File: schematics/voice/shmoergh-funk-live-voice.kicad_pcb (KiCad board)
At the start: 2 copper layers, 40 x 42 mm, 25 parts, among them Q1 2N3904, U1 TL074

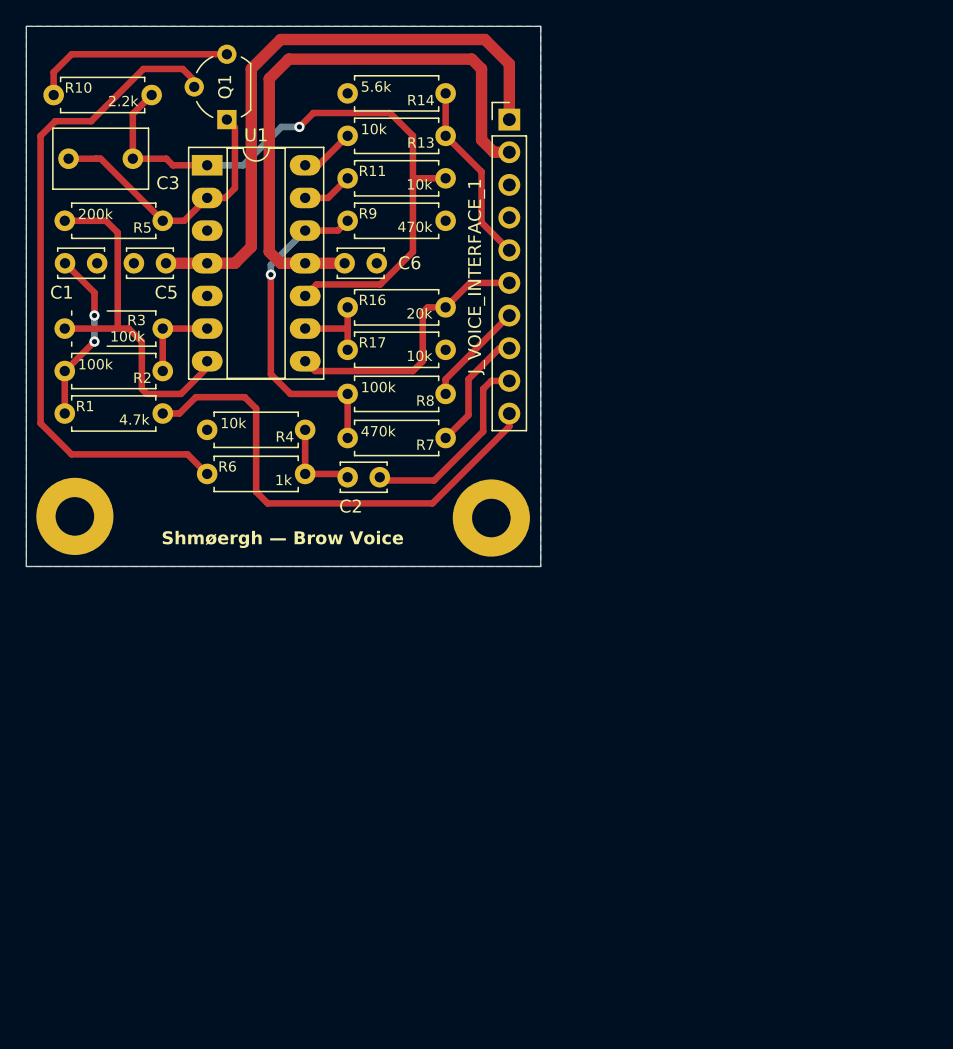
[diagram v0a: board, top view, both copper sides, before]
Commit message: Added digital ADSR (untested)
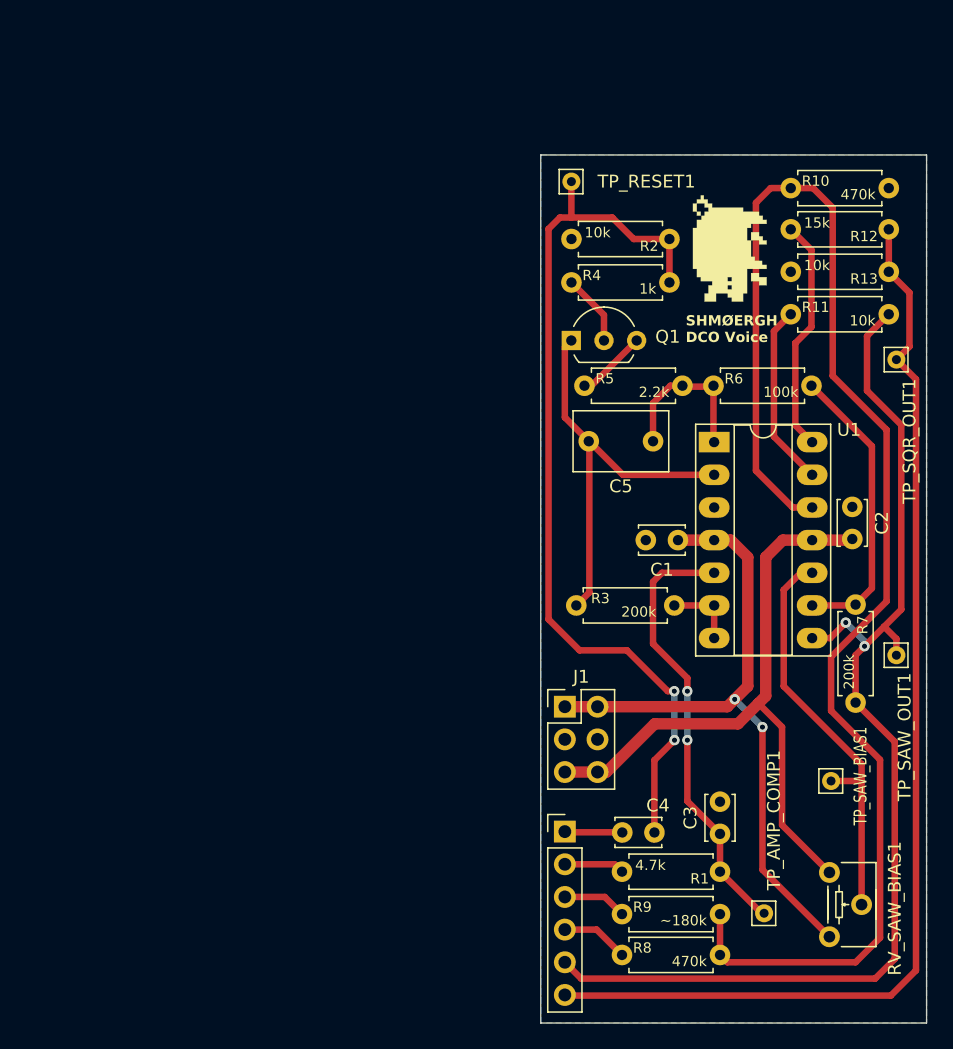
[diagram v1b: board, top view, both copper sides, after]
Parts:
- removed C6: 100n, Capacitor_THT:C_Disc_D3.4mm_W2.1mm_P2.50mm
- removed H1, H2: MountingHole, MountingHole:MountingHole_3mm_Pad
- removed R14: 5.6k, Shmoergh_Custom_Footprints:R_Axial_DIN0207_L6.3mm_D2.5mm_P7.62mm_Horizontal
- removed R16: 20k, Shmoergh_Custom_Footprints:R_Axial_DIN0207_L6.3mm_D2.5mm_P7.62mm_Horizontal
- removed R17: 10k, Shmoergh_Custom_Footprints:R_Axial_DIN0207_L6.3mm_D2.5mm_P7.62mm_Horizontal
- added C4: 560, Capacitor_THT:C_Disc_D3.4mm_W2.1mm_P2.50mm, F.Cu at (133.8, 102.7)
- added G***: LOGO, Shmoergh_Custom_Footprints:Gyeszno, F.Cu at (139.7, 57.3)
- added J1: Power, Connector_PinHeader_2.54mm:PinHeader_2x03_P2.54mm_Vertical, F.Cu at (126.9, 92.9)
- added R12: 15k, Shmoergh_Custom_Footprints:R_Axial_DIN0207_L6.3mm_D2.5mm_P7.62mm_Horizontal, F.Cu at (152.1, 55.8)
- added RV_SAW_BIAS1: 10k fine, PCM_Potentiometer_THT_AKL:Potentiometer_ACP_CA6-H2,5_Horizontal, F.Cu at (147.4, 105.8)
- added TP_AMP_COMP1: TestPoint, Connector_Pin:Pin_D0.7mm_L6.5mm_W1.8mm_FlatFork, F.Cu at (142.4, 109.0)
- added TP_RESET1: TestPoint, Connector_Pin:Pin_D0.7mm_L6.5mm_W1.8mm_FlatFork, F.Cu at (127.4, 52.1)
- added TP_SAW_BIAS1: TestPoint, Connector_Pin:Pin_D0.7mm_L6.5mm_W1.8mm_FlatFork, F.Cu at (147.6, 98.7)
- added TP_SAW_OUT1: TestPoint, Connector_Pin:Pin_D0.7mm_L6.5mm_W1.8mm_FlatFork, F.Cu at (152.7, 88.9)
- added TP_SQR_OUT1: TestPoint, Connector_Pin:Pin_D0.7mm_L6.5mm_W1.8mm_FlatFork, F.Cu at (152.7, 65.9)
- C2: value 270p -> 100n
- C3: value 1n (foil) -> 100n; footprint Capacitor_THT:C_Rect_L7.2mm_W4.5mm_P5.00mm_FKS2_FKP2_MKS2_MKP2 -> Capacitor_THT:C_Disc_D3.4mm_W2.1mm_P2.50mm
- C5: value 100n -> 1n (foil); footprint Capacitor_THT:C_Disc_D3.4mm_W2.1mm_P2.50mm -> Capacitor_THT:C_Rect_L7.2mm_W4.5mm_P5.00mm_FKS2_FKP2_MKS2_MKP2
- J_VOICE_INTERFACE_1: value Conn_01x10 -> Conn_01x06; footprint Connector_PinHeader_2.54mm:PinHeader_1x10_P2.54mm_Vertical -> Connector_PinHeader_2.54mm:PinHeader_1x06_P2.54mm_Vertical
- Q1: value 2N3904 -> 2N3906; footprint Package_TO_SOT_THT:TO-92_Wide -> PCM_Package_TO_SOT_THT_AKL:TO-92L_Inline_Wide
- R10: value 2.2k -> 470k
- R2: value 100k -> 10k
- R3: value 100k -> 200k
- R4: value 10k -> 1k
- R5: value 200k -> 2.2k
- R6: value 1k -> 100k
- R7: value 470k -> 200k
- R8: value 100k -> 470k
- R9: value 470k -> ~180k
- moved C3 69.6 mm to (138.9, 102.8), turned to 90 degrees
- moved R1 62.2 mm to (138.9, 105.7), turned to 180 degrees
- moved R9 58.0 mm to (131.3, 109.0)
- moved R10 57.8 mm to (144.4, 52.6)
- moved J_VOICE_INTERFACE_1 55.5 mm to (126.9, 102.6)
- moved C1 52.3 mm to (135.7, 80.0), turned to 180 degrees
- moved R8 45.7 mm to (131.3, 112.2), turned to 0 degrees
- moved R3 45.2 mm to (127.8, 85.0)
- moved U1 44.9 mm to (138.5, 72.3)
- moved R2 40.7 mm to (135.0, 56.5)
- moved C5 40.3 mm to (133.7, 72.3)
- moved R6 40.0 mm to (138.4, 67.9)
- moved C2 39.3 mm to (149.2, 77.4), turned to -90 degrees
- moved R11 36.0 mm to (144.4, 62.4)
- moved R13 36.0 mm to (152.1, 59.1)
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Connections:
- C1 pad 1: Net-(C1-Pad1) -> +12V
- C2 pad 1: Net-(C2-Pad1) -> GND
- C2 pad 2: RESET -> -12V
- C3 pad 1: Net-(U1C-+) -> Net-(U1B-+)
- C3 pad 2: Net-(Q1-E) -> GND
- C5 pad 1: +12V -> Net-(C5-Pad1)
- C5 pad 2: GND -> Net-(Q1-E)
- J_VOICE_INTERFACE_1 pad 1: +12V -> RESET
- J_VOICE_INTERFACE_1 pad 2: -12V -> AMP
- J_VOICE_INTERFACE_1 pad 3: GND -> PULSE_WIDTH
- J_VOICE_INTERFACE_1 pad 4: unconnected-(J_VOICE_INTERFACE_1-Pin_4-Pad4) -> PWM
- J_VOICE_INTERFACE_1 pad 5: SQR_OUT -> SAW_OUT
- J_VOICE_INTERFACE_1 pad 6: SAW_OUT -> SQR_OUT
- R1 pad 1: Net-(C1-Pad1) -> Net-(U1B-+)
- R10 pad 1: Net-(Q1-C) -> Net-(U1D-+)
- R10 pad 2: Net-(U1C-+) -> GND
- R11 pad 2: Net-(U1C-+) -> SAW_OUT
- R13 pad 2: Net-(R13-Pad2) -> GND
- R2 pad 1: Net-(U1B--) -> Net-(C4-Pad1)
- R2 pad 2: Net-(C1-Pad1) -> GND
- R3 pad 1: Net-(R3-Pad1) -> Net-(Q1-E)
- R4 pad 1: Net-(C2-Pad1) -> Net-(Q1-B)
- R4 pad 2: GND -> Net-(C4-Pad1)
- R5 pad 1: Net-(Q1-E) -> Net-(Q1-C)
- R5 pad 2: Net-(R3-Pad1) -> Net-(C5-Pad1)
- R6 pad 1: Net-(Q1-B) -> Net-(C5-Pad1)
- R6 pad 2: Net-(C2-Pad1) -> Net-(U1C--)
- R7 pad 1: PWM -> Net-(U1C--)
- R7 pad 2: Net-(U1D-+) -> SAW_OUT
- R8 pad 1: PULSE_WIDTH -> PWM
- R9 pad 1: Net-(U1D-+) -> PULSE_WIDTH
- R9 pad 2: GND -> Net-(U1D-+)
- U1 pad 1: Net-(U1C-+) -> Net-(C5-Pad1)
- U1 pad 14: Net-(R13-Pad2) -> Net-(R12-Pad2)
- U1 pad 5: GND -> Net-(U1B-+)
- U1 pad 7: Net-(R3-Pad1) -> Net-(U1B--)
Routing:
- net Net-(U1D-+): track 25.9 -> 112.0 mm, vias 1 -> 0
- net SQR_OUT: track 14.2 -> 87.5 mm
- net Net-(C4-Pad1): track 0.00 -> 70.7 mm, vias 0 -> 2
- net SAW_OUT: track 21.3 -> 89.7 mm, vias 0 -> 2
- net Net-(Q1-B): track 51.9 -> 5.56 mm
- net Net-(U1B-+): track 0.00 -> 34.5 mm, vias 0 -> 2
- net AMP: track 38.2 -> 4.68 mm
- net Net-(R3-Pad1): track 28.7 -> 0.00 mm
- net Net-(U1C-+): track 51.2 -> 32.1 mm, vias 1 -> 0
- net Net-(R12-Pad2): track 0.00 -> 18.3 mm
- net Net-(U1C--): track 6.60 -> 22.9 mm
- net Net-(C1-Pad1): track 13.6 -> 0.00 mm, vias 2 -> 0
- net Net-(C5-Pad1): track 0.00 -> 12.7 mm
- net Net-(Q1-E): track 21.6 -> 32.9 mm
- net RESET: track 15.3 -> 4.49 mm
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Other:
- board size 40 x 42 mm -> 30 x 67.5 mm
- board text added: "SHMØERGH DCO Voice"
- board text removed: "Shmøergh — Brow Voice"

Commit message: Updated schem. + added JLCPCB gerbers
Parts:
- removed G***: LOGO, Shmoergh_Custom_Footprints:Gyeszno
- R10: value 470k -> 330k
- R11: value 10k -> 100k
- R9: value ~180k -> 470k
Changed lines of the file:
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@@
         (effects (font (size 0.8 0.8) (thickness 0.15)) (justify left))
     )
-    (fp_text value "470k" (at 6.6 0.5) (layer "F.SilkS")
+    (fp_text value "330k" (at 6.6 0.5) (layer "F.SilkS")
         (effects (font (size 0.8 0.8) (thickness 0.15)) (justify right))
     )
@@
         (effects (font (size 0.8 0.8) (thickness 0.15)) (justify left))
     )
-    (fp_text value "10k" (at 6.6 0.5) (layer "F.SilkS")
+    (fp_text value "100k" (at 6.6 0.5) (layer "F.SilkS")
         (effects (font (size 0.8 0.8) (thickness 0.15)) (justify right))
     )
@@
     )
   )
-  (footprint "Shmoergh_Custom_Footprints:Gyeszno" (layer "F.Cu")
-    (at 139.7 57.277 90)
-    (attr through_hole)
-    (fp_text reference "G***" (at 0 0 90) (layer "F.SilkS") hide
-        (effects (font (size 1.524 1.524) (thickness 0.3)))
-    )
-    (fp_text value "LOGO" (at 0.75 0 90) (layer "F.SilkS") hide
-        (effects (font (size 1.524 1.524) (thickness 0.3)))
-    )
-    (fp_poly
-      (pts
-        (xy 2.8702 -2.8702)
-        (xy 3.5052 -2.8702)
-        (xy 3.5052 -2.5654)
-        (xy 2.8702 -2.5654)
-        (xy 2.8702 -2.8702)
-      )
-      (stroke (width 0.01) (type solid)) (fill solid) (layer "F.SilkS"))
-    (fp_poly
-      (pts
-        (xy 2.8702 -2.2606)
-        (xy 2.5527 -2.2606)
-        (xy 2.5527 -2.5654)
-        (xy 2.8702 -2.5654)
-        (xy 2.8702 -2.2606)
-      )
-      (stroke (width 0.01) (type solid)) (fill solid) (layer "F.SilkS"))
-    (fp_poly
-      (pts
-        (xy -1.905 2.2733)
-        (xy -2.2225 2.2733)
-        (xy -2.2225 2.8702)
-        (xy -2.8575 2.8702)
-        (xy -2.8575 2.2733)
-        (xy -2.54 2.2733)
-        (xy -2.54 1.651)
-        (xy -1.905 1.651)
-        (xy -1.905 2.2733)
-      )
-      (stroke (width 0.01) (type solid)) (fill solid) (layer "F.SilkS"))
-    (fp_poly
-      (pts
-        (xy 1.27 2.2733)
-        (xy 0.9525 2.2733)
-        (xy 0.9525 2.5654)
-        (xy 0.635 2.5654)
-        (xy 0.635 2.8702)
-        (xy 0.3175 2.8702)
-        (xy 0.3175 2.2733)
-        (xy 0.635 2.2733)
-        (xy 0.635 1.651)
-        (xy 1.27 1.651)
-        (xy 1.27 2.2733)
-      )
-      (stroke (width 0.01) (type solid)) (fill solid) (layer "F.SilkS"))
-    (fp_poly
-      (pts
-        (xy 1.6002 -2.5654)
-        (xy 2.2352 -2.5654)
-        (xy 2.2352 -2.2098)
-        (xy 2.5527 -2.2098)
-        (xy 2.5527 -1.9685)
-        (xy 2.8702 -1.9685)
-        (xy 2.8702 -1.6637)
-        (xy 3.1877 -1.6637)
-        (xy 3.1877 -1.9685)
-        (xy 3.5052 -1.9685)
-        (xy 3.5052 -2.5654)
-        (xy 3.8227 -2.5654)
-        (xy 3.8227 -2.2606)
-        (xy 4.1402 -2.2606)
-        (xy 4.1402 -2.0193)
-        (xy 3.8227 -2.0193)
-        (xy 3.8227 -1.7145)
-        (xy 3.5052 -1.7145)
-        (xy 3.5052 -1.3716)
-        (xy 3.1877 -1.3716)
-        (xy 3.1877 1.0414)
-        (xy 2.8702 1.0414)
-        (xy 2.8702 2.2733)
-        (xy 2.5527 2.2733)
-        (xy 2.5527 2.5654)
-        (xy 2.2352 2.5654)
-        (xy 2.2352 2.8702)
-        (xy 1.9177 2.8702)
-        (xy 1.9177 1.651)
-        (xy 1.6002 1.651)
-        (xy 1.6002 1.3462)
-        (xy 0.635 1.3462)
-        (xy 0.635 1.651)
-        (xy -0.635 1.651)
-        (xy -0.635 1.9431)
-        (xy -0.9525 1.9431)
-        (xy -0.9525 2.5146)
-        (xy -1.27 2.5146)
-        (xy -1.27 2.8702)
-        (xy -1.5875 2.8702)
-        (xy -1.5875 1.3462)
-        (xy -3.4925 1.3462)
-        (xy -3.4925 1.0414)
-        (xy -4.1275 1.0414)
-        (xy -4.1275 0.1524)
-        (xy -3.81 0.1524)
-        (xy -3.81 -0.1651)
-        (xy -3.4925 -0.1651)
-        (xy -3.175 -0.1651)
-        (xy -3.175 0.1524)
-        (xy -2.8575 0.1524)
-        (xy -2.8575 -0.1651)
-        (xy -2.54 -0.1651)
-        (xy -2.54 0.1524)
-        (xy -2.2225 0.1524)
-        (xy -2.2225 -0.1651)
-        (xy -2.54 -0.1651)
-        (xy -2.8575 -0.1651)
-        (xy -3.175 -0.1651)
-        (xy -3.4925 -0.1651)
-        (xy -3.4925 -1.0668)
-        (xy -4.1275 -1.0668)
-        (xy -4.1275 -1.9685)
-        (xy -3.4925 -1.9685)
-        (xy -3.4925 -1.6637)
-        (xy -2.8575 -1.6637)
-        (xy -2.8575 -1.3716)
-        (xy -2.54 -1.3716)
-        (xy -2.54 -2.2606)
-        (xy -2.2225 -2.2606)
-        (xy -2.2225 -2.5654)
-        (xy -1.5875 -2.5654)
-        (xy -1.5875 -2.8702)
-        (xy 1.6002 -2.8702)
-        (xy 1.6002 -2.5654)
-      )
-      (stroke (width 0.01) (type solid)) (fill solid) (layer "F.SilkS"))
-  )
   (footprint "Connector_Pin:Pin_D0.7mm_L6.5mm_W1.8mm_FlatFork" (layer "F.Cu")
     (at 127.381 52.07)
@@
         (effects (font (size 0.8 0.8) (thickness 0.15)) (justify left))
     )
-    (fp_text value "~180k" (at 6.6 0.5) (layer "F.SilkS")
+    (fp_text value "470k" (at 6.6 0.5) (layer "F.SilkS")
         (effects (font (size 0.8 0.8) (thickness 0.15)) (justify right))
     )
